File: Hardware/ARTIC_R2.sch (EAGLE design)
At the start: 117 parts, among them J1 U.FL, J2 THING_PLUS, J5 Flash Programming, K1 TLP3475R, Q1 3.1A/30V/105mΩ, U1 2Mbit SPI Flash, U2 1.8V/100mA, U3 ARTIC_R2, U4 RFPA0133, U5 AS179-92LF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

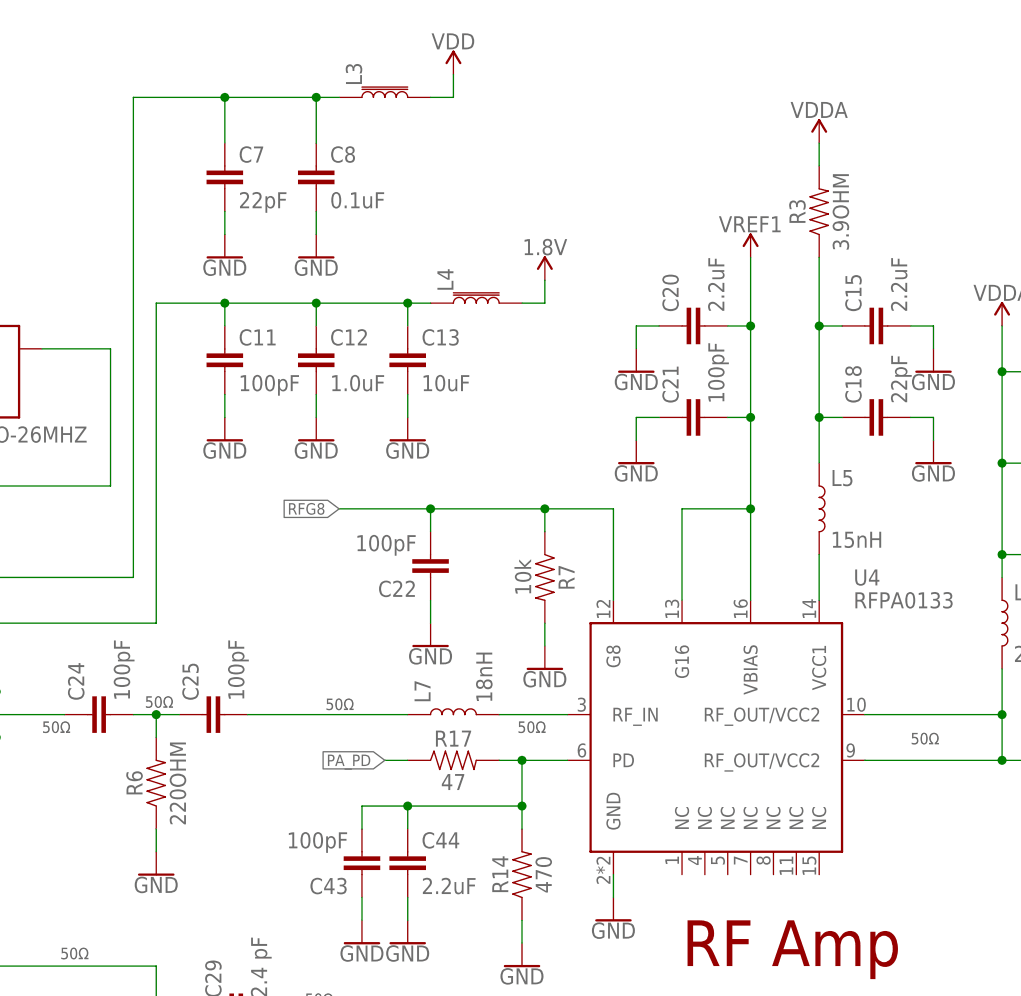
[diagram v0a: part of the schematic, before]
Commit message: Update Eagle files - remove New_Parts.lbr
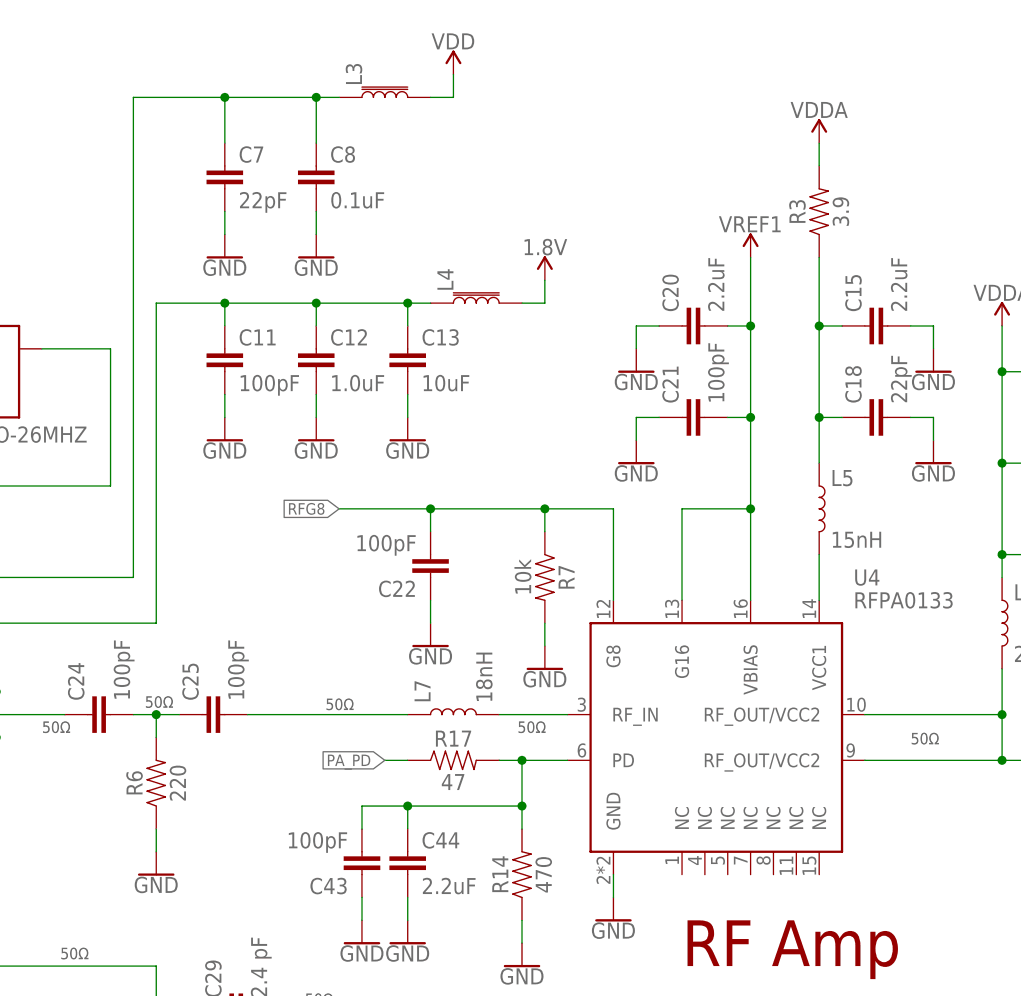
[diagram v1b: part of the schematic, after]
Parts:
- C28: device New_Parts_Capacitors:9.1PF-0402-TIGHT -> SparkFun-Capacitors:9.1PF-0402-TIGHT
- K1: device New_Parts_DiscreteSemi:TLP3475R -> SparkFun-DiscreteSemi:TLP3475R
- L11: device New_Parts_Coils:30NH-0402 -> SparkFun-Coils:30NH-0402
- L12: device New_Parts_Coils:51NH-0402 -> SparkFun-Coils:51NH-0402
- L5: device New_Parts_Coils:15NH-0402 -> SparkFun-Coils:15NH-0402
- L6: device New_Parts_Coils:27NH-0402 -> SparkFun-Coils:27NH-0402
- L7: device New_Parts_Coils:18NH-0402 -> SparkFun-Coils:18NH-0402
- L8: device New_Parts_Coils:12NH-0402 -> SparkFun-Coils:12NH-0402
- R14: device New_Parts_Resistors:470OHM-0402-TIGHT-1/16W-1% -> SparkFun-Resistors:470OHM-0402-TIGHT-1/16W-1%
- R17: device New_Parts_Resistors:47OHM-0402-TIGHT-1/16W-1% -> SparkFun-Resistors:47OHM-0402-TIGHT-1/16W-1%
- R3: value 3.9OHM -> 3.9; device New_Parts_Resistors:3.9OHM -> SparkFun-Resistors:3.9OHM-0402-TIGHT-1/16W-1%
- R6: value 220OHM -> 220; device New_Parts_Resistors:220OHM -> SparkFun-Resistors:220OHM-0402-TIGHT-1/16W-1%
- U1: device New_Parts_IC-Memory:SST25VF020BSMD -> SparkFun-IC-Memory:SST25VF020BSO08_INDUSTRIAL_TEMP
- U3: device New_Parts_IC-Comms:ARTIC_R2 -> SparkFun-RF:ARTIC_R2
- U4: device New_Parts_IC-Comms:RFPA0133 -> SparkFun-RF:RFPA0133
- U5: device New_Parts_IC-Comms:AS179-92LF -> SparkFun-RF:AS179-92LF
- U6: device New_Parts_IC-Power:V_REG_LP5907SOT23-3.0V -> SparkFun-IC-Power:V_REG_LP5907SOT23-3.0V
- X1: device New_Parts_Clocks:CRYSTAL-TCXO-26MHZ -> SparkFun-Clocks:CRYSTAL-TCXO-26MHZ
